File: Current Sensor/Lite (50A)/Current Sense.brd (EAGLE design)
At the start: 17.8 x 19 mm, 13 parts, among them IC1 INA169

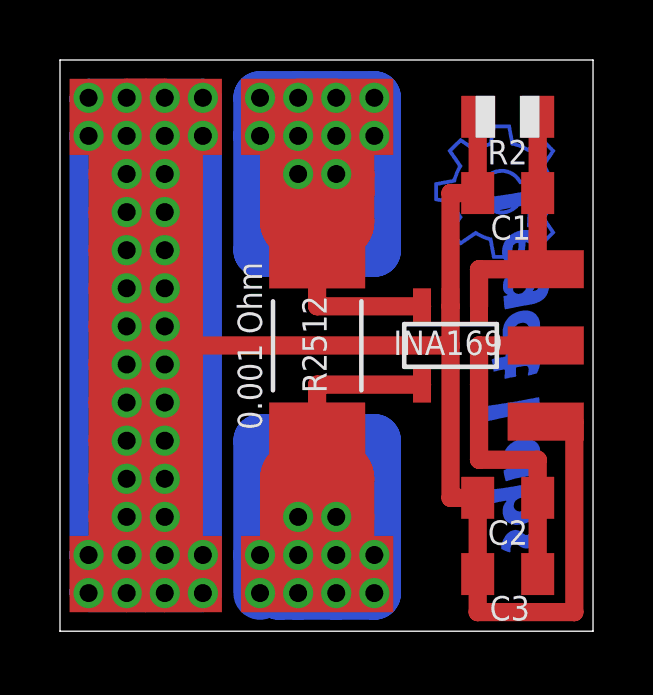
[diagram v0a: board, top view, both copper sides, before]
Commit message: Changed Current Sensors
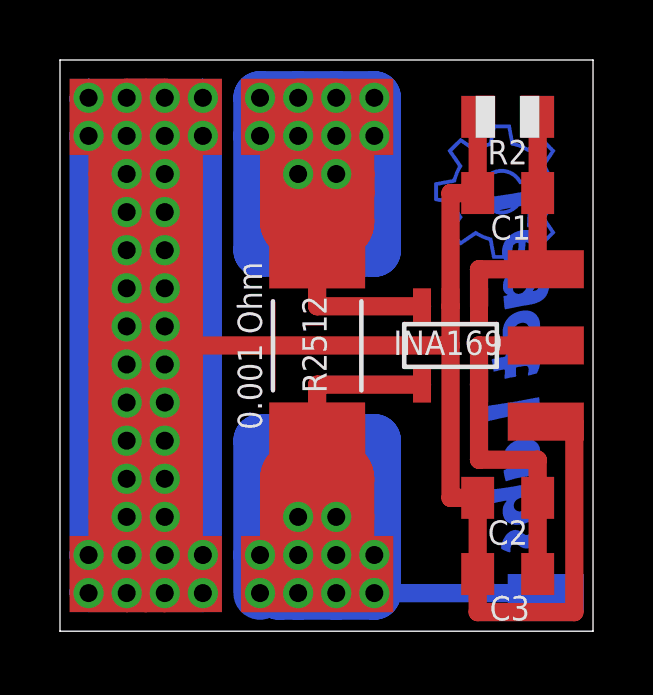
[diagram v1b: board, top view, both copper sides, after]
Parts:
- added VOLTAGE: (no value), wirepad:SMD1,27-2,54
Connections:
- net IN renamed N$2
- net OUT: now also VOLTAGE.1
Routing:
- net OUT: track 49.1 -> 54.8 mm
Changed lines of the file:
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@@
 <attribute name="VALUE" x="5.3975" y="12.192" size="1.27" layer="27" rot="R270"/>
 </element>
+<element name="VOLTAGE" library="wirepad" package="SMD1,27-2,54" value="" x="16.1925" y="1.27" rot="MR90"/>
 </elements>
 <signals>
@@
 <wire x1="8.5725" y1="1.27" x2="6.6675" y2="1.27" width="0.8128" layer="1"/>
 <wire x1="8.5725" y1="8.219" x2="8.5725" y2="6.725" width="0.6096" layer="1"/>
-<wire x1="8.5725" y1="6.6675" x2="8.5725" y2="6.725" width="0" layer="19" extent="1-1"/>
-</signal>
-<signal name="IN">
-<contactref element="IC1" pad="3"/>
-<contactref element="PAD3" pad="1"/>
-<wire x1="7.9375" y1="13.6652" x2="7.9375" y2="15.24" width="2.54" layer="1"/>
-<wire x1="7.9375" y1="15.24" x2="7.9375" y2="16.51" width="2.54" layer="1"/>
-<wire x1="7.9375" y1="16.51" x2="7.9375" y2="17.145" width="2.54" layer="1"/>
-<wire x1="7.9375" y1="17.145" x2="8.5725" y2="17.145" width="2.54" layer="1"/>
-<wire x1="8.5725" y1="17.145" x2="9.2075" y2="17.145" width="2.54" layer="1"/>
-<wire x1="9.2075" y1="17.145" x2="9.2075" y2="16.51" width="2.54" layer="1"/>
-<wire x1="9.2075" y1="16.51" x2="9.2075" y2="15.24" width="2.54" layer="1"/>
-<wire x1="9.2075" y1="15.24" x2="9.2075" y2="14.605" width="2.54" layer="1"/>
-<wire x1="9.2075" y1="14.605" x2="8.5725" y2="14.605" width="2.54" layer="1"/>
-<wire x1="8.5725" y1="14.605" x2="8.5725" y2="13.97" width="2.54" layer="1"/>
-<wire x1="8.5725" y1="14.605" x2="8.5725" y2="17.145" width="2.54" layer="1"/>
-<wire x1="12.0675" y1="10.831" x2="8.5725" y2="10.831" width="0.6096" layer="1"/>
-<wire x1="8.5725" y1="10.831" x2="8.5725" y2="12.325" width="0.6096" layer="1"/>
-<wire x1="8.5725" y1="12.325" x2="8.5725" y2="17.145" width="0.6096" layer="1"/>
-<wire x1="6.6675" y1="17.78" x2="7.9375" y2="17.78" width="1.778" layer="16"/>
-<wire x1="7.9375" y1="17.78" x2="9.2075" y2="17.78" width="1.778" layer="16"/>
-<wire x1="9.2075" y1="17.78" x2="10.4775" y2="17.78" width="1.778" layer="16"/>
-<wire x1="6.6675" y1="17.78" x2="6.6675" y2="16.51" width="1.778" layer="16"/>
-<wire x1="6.6675" y1="16.51" x2="6.6675" y2="12.7" width="1.778" layer="16"/>
-<wire x1="6.6675" y1="12.7" x2="10.4775" y2="12.7" width="1.778" layer="16"/>
-<wire x1="10.4775" y1="12.7" x2="10.4775" y2="16.51" width="1.778" layer="16"/>
-<wire x1="10.4775" y1="17.78" x2="10.4775" y2="16.51" width="1.778" layer="16"/>
-<wire x1="10.4775" y1="16.51" x2="9.2075" y2="16.51" width="1.778" layer="16"/>
-<wire x1="9.2075" y1="16.51" x2="7.9375" y2="16.51" width="1.778" layer="16"/>
-<wire x1="7.9375" y1="16.51" x2="7.9375" y2="15.24" width="1.778" layer="16"/>
-<wire x1="7.9375" y1="15.24" x2="7.9375" y2="13.97" width="1.778" layer="16"/>
-<wire x1="7.9375" y1="13.97" x2="9.2075" y2="13.97" width="1.778" layer="16"/>
-<wire x1="9.2075" y1="13.97" x2="9.2075" y2="15.24" width="1.778" layer="16"/>
-<via x="6.6675" y="17.78" extent="1-16" drill="0.6"/>
-<via x="7.9375" y="17.78" extent="1-16" drill="0.6"/>
-<via x="9.2075" y="17.78" extent="1-16" drill="0.6"/>
-<via x="10.4775" y="17.78" extent="1-16" drill="0.6"/>
-<via x="10.4775" y="16.51" extent="1-16" drill="0.6"/>
-<via x="9.2075" y="16.51" extent="1-16" drill="0.6"/>
-<via x="7.9375" y="16.51" extent="1-16" drill="0.6"/>
-<via x="6.6675" y="16.51" extent="1-16" drill="0.6"/>
-<via x="7.9375" y="15.24" extent="1-16" drill="0.6"/>
-<via x="9.2075" y="15.24" extent="1-16" drill="0.6"/>
-<contactref element="R1" pad="1"/>
-<wire x1="9.2075" y1="15.24" x2="9.2075" y2="13.6525" width="2.54" layer="1"/>
-<wire x1="9.2075" y1="13.6525" x2="7.9375" y2="13.6525" width="2.54" layer="1"/>
+<contactref element="VOLTAGE" pad="1"/>
+<wire x1="8.5725" y1="6.725" x2="8.5725" y2="6.6675" width="0" layer="19" extent="1-1"/>
+<wire x1="16.1925" y1="1.27" x2="10.4775" y2="1.27" width="0.6096" layer="16"/>
 </signal>
 <signal name="N$4">
@@
 <wire x1="9.8425" y1="14.605" x2="9.525" y2="14.605" width="1.27" layer="1"/>
 </signal>
+<signal name="N$2">
+<contactref element="IC1" pad="3"/>
+<contactref element="PAD3" pad="1"/>
+<contactref element="R1" pad="1"/>
+<wire x1="7.9375" y1="13.6652" x2="7.9375" y2="15.24" width="2.54" layer="1"/>
+<wire x1="7.9375" y1="15.24" x2="7.9375" y2="16.51" width="2.54" layer="1"/>
+<wire x1="7.9375" y1="16.51" x2="7.9375" y2="17.145" width="2.54" layer="1"/>
+<wire x1="7.9375" y1="17.145" x2="8.5725" y2="17.145" width="2.54" layer="1"/>
+<wire x1="8.5725" y1="17.145" x2="9.2075" y2="17.145" width="2.54" layer="1"/>
+<wire x1="9.2075" y1="17.145" x2="9.2075" y2="16.51" width="2.54" layer="1"/>
+<wire x1="9.2075" y1="16.51" x2="9.2075" y2="15.24" width="2.54" layer="1"/>
+<wire x1="9.2075" y1="15.24" x2="9.2075" y2="14.605" width="2.54" layer="1"/>
+<wire x1="9.2075" y1="14.605" x2="8.5725" y2="14.605" width="2.54" layer="1"/>
+<wire x1="8.5725" y1="14.605" x2="8.5725" y2="13.97" width="2.54" layer="1"/>
+<wire x1="8.5725" y1="14.605" x2="8.5725" y2="17.145" width="2.54" layer="1"/>
+<wire x1="12.0675" y1="10.831" x2="8.5725" y2="10.831" width="0.6096" layer="1"/>
+<wire x1="8.5725" y1="10.831" x2="8.5725" y2="12.325" width="0.6096" layer="1"/>
+<wire x1="8.5725" y1="12.325" x2="8.5725" y2="17.145" width="0.6096" layer="1"/>
+<wire x1="6.6675" y1="17.78" x2="7.9375" y2="17.78" width="1.778" layer="16"/>
+<wire x1="7.9375" y1="17.78" x2="9.2075" y2="17.78" width="1.778" layer="16"/>
+<wire x1="9.2075" y1="17.78" x2="10.4775" y2="17.78" width="1.778" layer="16"/>
+<wire x1="6.6675" y1="17.78" x2="6.6675" y2="16.51" width="1.778" layer="16"/>
+<wire x1="6.6675" y1="16.51" x2="6.6675" y2="12.7" width="1.778" layer="16"/>
+<wire x1="6.6675" y1="12.7" x2="10.4775" y2="12.7" width="1.778" layer="16"/>
+<wire x1="10.4775" y1="12.7" x2="10.4775" y2="16.51" width="1.778" layer="16"/>
+<wire x1="10.4775" y1="17.78" x2="10.4775" y2="16.51" width="1.778" layer="16"/>
+<wire x1="10.4775" y1="16.51" x2="9.2075" y2="16.51" width="1.778" layer="16"/>
+<wire x1="9.2075" y1="16.51" x2="7.9375" y2="16.51" width="1.778" layer="16"/>
+<wire x1="7.9375" y1="16.51" x2="7.9375" y2="15.24" width="1.778" layer="16"/>
+<wire x1="7.9375" y1="15.24" x2="7.9375" y2="13.97" width="1.778" layer="16"/>
+<wire x1="7.9375" y1="13.97" x2="9.2075" y2="13.97" width="1.778" layer="16"/>
+<wire x1="9.2075" y1="13.97" x2="9.2075" y2="15.24" width="1.778" layer="16"/>
+<via x="6.6675" y="17.78" extent="1-16" drill="0.6"/>
+<via x="7.9375" y="17.78" extent="1-16" drill="0.6"/>
+<via x="9.2075" y="17.78" extent="1-16" drill="0.6"/>
+<via x="10.4775" y="17.78" extent="1-16" drill="0.6"/>
+<via x="10.4775" y="16.51" extent="1-16" drill="0.6"/>
+<via x="9.2075" y="16.51" extent="1-16" drill="0.6"/>
+<via x="7.9375" y="16.51" extent="1-16" drill="0.6"/>
+<via x="6.6675" y="16.51" extent="1-16" drill="0.6"/>
+<via x="7.9375" y="15.24" extent="1-16" drill="0.6"/>
+<via x="9.2075" y="15.24" extent="1-16" drill="0.6"/>
+<wire x1="9.2075" y1="15.24" x2="9.2075" y2="13.6525" width="2.54" layer="1"/>
+<wire x1="9.2075" y1="13.6525" x2="7.9375" y2="13.6525" width="2.54" layer="1"/>
+</signal>
 </signals>
